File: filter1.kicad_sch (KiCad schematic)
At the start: 10 parts

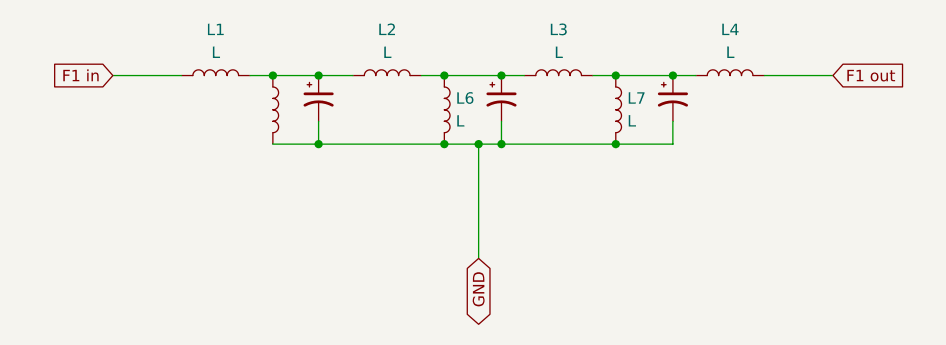
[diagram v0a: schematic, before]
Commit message: v0.2 passes ERC & DRC except for no solder mask between pads on SOT89
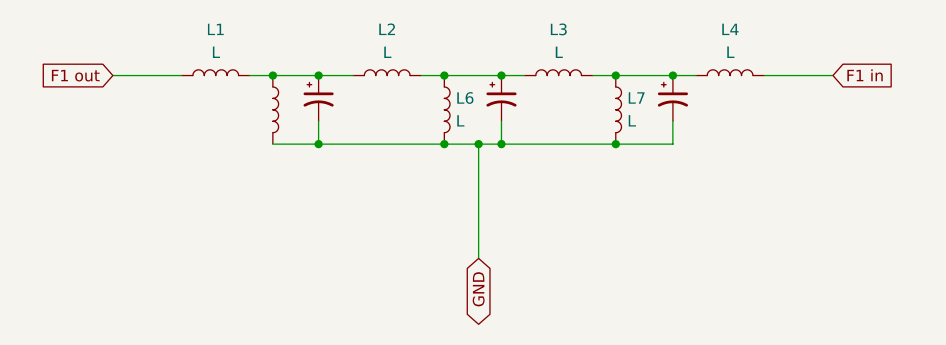
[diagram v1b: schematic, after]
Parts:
- C1, C2, C3: footprint (none) -> Capacitor_SMD:C_1210_3225Metric
- L1, L2, L3, L4, L5, L6, L7: footprint (none) -> Inductor_SMD:L_1210_3225Metric
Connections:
- net F1 in: now also L4.2; no longer L1.1
- net F1 out: now also L1.1; no longer L4.2
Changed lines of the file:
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@@
     )
   )
-  (global_label "F1 in" (shape input) (at 106.68 72.39 180) (fields_autoplaced)
+  (global_label "F1 out" (shape input) (at 106.68 72.39 180) (fields_autoplaced)
     (effects (font (size 1.27 1.27)) (justify right))
-    (property "Intersheetrefs" "${INTERSHEET_REFS}" (at 99.4089 72.39 0)
+    (property "Intersheetrefs" "${INTERSHEET_REFS}" (at 98.139 72.39 0)
       (effects (font (size 1.27 1.27)) (justify right) hide)
     )
   )
-  (global_label "F1 out" (shape input) (at 186.69 72.39 0) (fields_autoplaced)
+  (global_label "F1 in" (shape input) (at 186.69 72.39 0) (fields_autoplaced)
     (effects (font (size 1.27 1.27)) (justify left))
-    (property "Intersheetrefs" "${INTERSHEET_REFS}" (at 195.231 72.39 0)
+    (property "Intersheetrefs" "${INTERSHEET_REFS}" (at 193.9611 72.39 0)
       (effects (font (size 1.27 1.27)) (justify left) hide)
     )
@@
       (effects (font (size 1.27 1.27)))
     )
-    (property "Footprint" "" (at 137.16 72.39 0)
+    (property "Footprint" "Inductor_SMD:L_1210_3225Metric" (at 137.16 72.39 0)
       (effects (font (size 1.27 1.27)) hide)
     )
@@
       (effects (font (size 1.27 1.27)))
     )
-    (property "Footprint" "" (at 175.26 72.39 0)
+    (property "Footprint" "Inductor_SMD:L_1210_3225Metric" (at 175.26 72.39 0)
       (effects (font (size 1.27 1.27)) hide)
     )
@@
       (effects (font (size 1.27 1.27)))
     )
-    (property "Footprint" "" (at 156.21 72.39 0)
+    (property "Footprint" "Inductor_SMD:L_1210_3225Metric" (at 156.21 72.39 0)
       (effects (font (size 1.27 1.27)) hide)
     )
@@
       (effects (font (size 1.27 1.27)) (justify left) hide)
     )
-    (property "Footprint" "" (at 129.54 74.93 0)
+    (property "Footprint" "Capacitor_SMD:C_1210_3225Metric" (at 129.54 74.93 0)
       (effects (font (size 1.27 1.27)) hide)
     )
@@
       (effects (font (size 1.27 1.27)) (justify left) hide)
     )
-    (property "Footprint" "" (at 149.86 74.93 0)
+    (property "Footprint" "Capacitor_SMD:C_1210_3225Metric" (at 149.86 74.93 0)
       (effects (font (size 1.27 1.27)) hide)
     )
@@
       (effects (font (size 1.27 1.27)) (justify left))
     )
-    (property "Footprint" "" (at 143.51 76.2 0)
+    (property "Footprint" "Inductor_SMD:L_1210_3225Metric" (at 143.51 76.2 0)
       (effects (font (size 1.27 1.27)) hide)
     )
@@
       (effects (font (size 1.27 1.27)) (justify left) hide)
     )
-    (property "Footprint" "" (at 124.46 76.2 0)
+    (property "Footprint" "Inductor_SMD:L_1210_3225Metric" (at 124.46 76.2 0)
       (effects (font (size 1.27 1.27)) hide)
     )
@@
       (effects (font (size 1.27 1.27)) (justify left))
     )
-    (property "Footprint" "" (at 162.56 76.2 0)
+    (property "Footprint" "Inductor_SMD:L_1210_3225Metric" (at 162.56 76.2 0)
       (effects (font (size 1.27 1.27)) hide)
     )
@@
       (effects (font (size 1.27 1.27)) (justify left) hide)
     )
-    (property "Footprint" "" (at 168.91 74.93 0)
+    (property "Footprint" "Capacitor_SMD:C_1210_3225Metric" (at 168.91 74.93 0)
       (effects (font (size 1.27 1.27)) hide)
     )
@@
       (effects (font (size 1.27 1.27)))
     )
-    (property "Footprint" "" (at 118.11 72.39 0)
-      (effects (font (size 1.27 1.27)) hide)
-    )
+    (property "Footprint" "Inductor_SMD:L_1210_3225Metric" (at 118.11 72.39 0)
+      (effects (font (size 1.27 1.27)) hide)
+    )

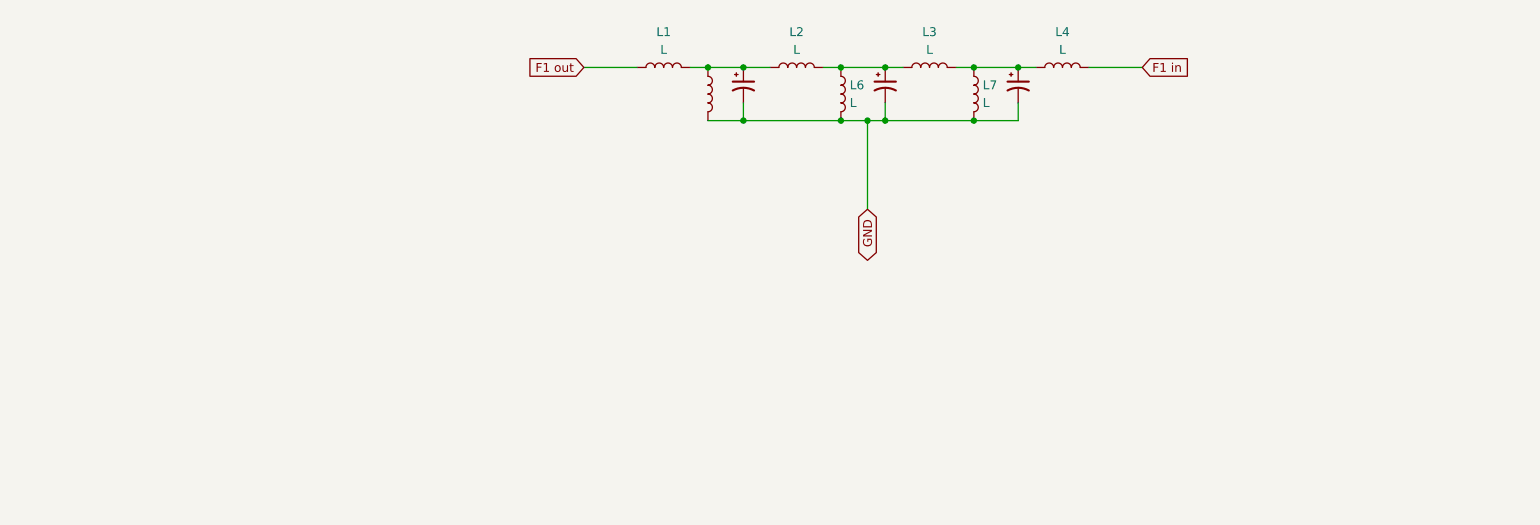
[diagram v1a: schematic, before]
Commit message: v0.3 added all four filters.  ERC pass, DRC struggling.  Need a ground plane
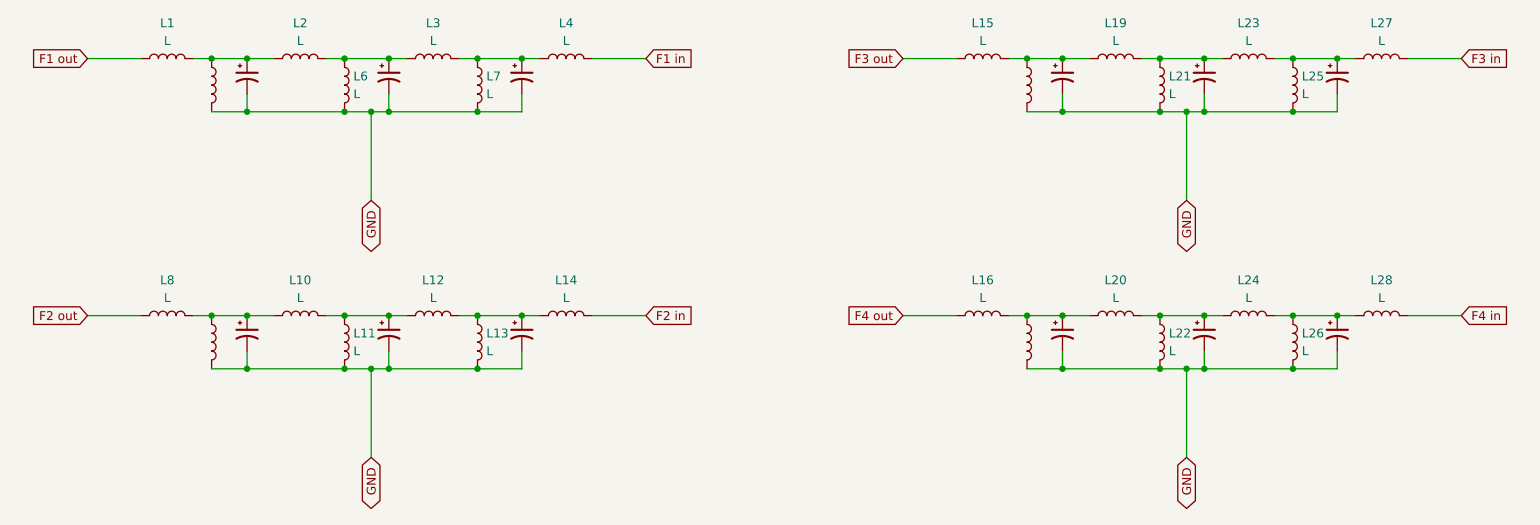
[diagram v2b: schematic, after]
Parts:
- added C10, C11, C12, C4, C5, C6, C7, C8, C9: C_Polarized_Small_US, Capacitor_SMD:C_1210_3225Metric, symbol Device:C_Polarized_Small_US
- added L10, L11, L12, L13, L14, L15, L16, L17, L18, L19, L20, L21, L22, L23, L24, L25, L26, L27, L28, L8, L9: L, Inductor_SMD:L_1210_3225Metric, symbol Device:L
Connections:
- net GND: now also C10.2, C11.2, C12.2, C4.2, C5.2, C6.2, C7.2, C8.2, C9.2, L11.2, L13.2, L17.2, L18.2, L21.2, L22.2, L25.2, L26.2, L9.2
- new net: C4.1, L10.1, L8.2, L9.1
- new net: C8.1, L16.2, L18.1, L20.1
- new net: C9.1, L19.2, L21.1, L23.1
- new net: C11.1, L23.2, L25.1, L27.1
- new net: C12.1, L24.2, L26.1, L28.1
- new net: C10.1, L20.2, L22.1, L24.1
- new net: C5.1, L10.2, L11.1, L12.1
- new net: C6.1, L12.2, L13.1, L14.1
- new net: C7.1, L15.2, L17.1, L19.1
- new net F2 in: L14.2
- new net F2 out: L8.1
- new net F3 in: L27.2
- new net F3 out: L15.1
- new net F4 in: L28.2
- new net F4 out: L16.1
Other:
- moved on the sheet: L1, L2, L3, L4, L6, L7

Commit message: v0.4 ERC/DRC pass; added missing caps; mounting holes; moved SMA & headers out and re-spaced filter chains
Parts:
- C1, C10, C11, C12, C2, C3, C4, C5, C6, C7, C8, C9: value C_Polarized_Small_US -> (none)
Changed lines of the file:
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@@
     (title "switched bandpass filter")
     (date "2023-07-22")
-    (rev "v0.3")
+    (rev "v0.4")
     (comment 1 "Copyright © 2023 WA7GIL")
   )
@@
       (effects (font (size 1.27 1.27)) (justify left) hide)
     )
-    (property "Value" "C_Polarized_Small_US" (at 177.8 111.3282 0)
+    (property "Value" " " (at 177.8 111.3282 0)
       (effects (font (size 1.27 1.27)) (justify left) hide)
     )
@@
       (effects (font (size 1.27 1.27)) (justify left) hide)
     )
-    (property "Value" "C_Polarized_Small_US" (at 198.12 74.4982 0)
+    (property "Value" " " (at 198.12 74.4982 0)
       (effects (font (size 1.27 1.27)) (justify left) hide)
     )
@@
       (effects (font (size 1.27 1.27)) (justify left) hide)
     )
-    (property "Value" "C_Polarized_Small_US" (at 217.17 111.3282 0)
+    (property "Value" " " (at 217.17 111.3282 0)
       (effects (font (size 1.27 1.27)) (justify left) hide)
     )
@@
       (effects (font (size 1.27 1.27)) (justify left) hide)
     )
-    (property "Value" "C_Polarized_Small_US" (at 100.33 111.3282 0)
+    (property "Value" " " (at 100.33 111.3282 0)
       (effects (font (size 1.27 1.27)) (justify left) hide)
     )
@@
       (effects (font (size 1.27 1.27)) (justify left) hide)
     )
-    (property "Value" "C_Polarized_Small_US" (at 217.17 74.4982 0)
+    (property "Value" " " (at 217.17 74.4982 0)
       (effects (font (size 1.27 1.27)) (justify left) hide)
     )
@@
       (effects (font (size 1.27 1.27)) (justify left) hide)
     )
-    (property "Value" "C_Polarized_Small_US" (at 60.96 74.4982 0)
+    (property "Value" " " (at 60.96 74.4982 0)
       (effects (font (size 1.27 1.27)) (justify left) hide)
     )
@@
       (effects (font (size 1.27 1.27)) (justify left) hide)
     )
-    (property "Value" "C_Polarized_Small_US" (at 81.28 74.4982 0)
+    (property "Value" " " (at 81.28 74.4982 0)
       (effects (font (size 1.27 1.27)) (justify left) hide)
     )
@@
       (effects (font (size 1.27 1.27)) (justify left) hide)
     )
-    (property "Value" "C_Polarized_Small_US" (at 81.28 111.3282 0)
+    (property "Value" " " (at 81.28 111.3282 0)
       (effects (font (size 1.27 1.27)) (justify left) hide)
     )
@@
       (effects (font (size 1.27 1.27)) (justify left) hide)
     )
-    (property "Value" "C_Polarized_Small_US" (at 100.33 74.4982 0)
+    (property "Value" " " (at 100.33 74.4982 0)
       (effects (font (size 1.27 1.27)) (justify left) hide)
     )
@@
       (effects (font (size 1.27 1.27)) (justify left) hide)
     )
-    (property "Value" "C_Polarized_Small_US" (at 60.96 111.3282 0)
+    (property "Value" " " (at 60.96 111.3282 0)
       (effects (font (size 1.27 1.27)) (justify left) hide)
     )
@@
       (effects (font (size 1.27 1.27)) (justify left) hide)
     )
-    (property "Value" "C_Polarized_Small_US" (at 177.8 74.4982 0)
+    (property "Value" " " (at 177.8 74.4982 0)
       (effects (font (size 1.27 1.27)) (justify left) hide)
     )
@@
       (effects (font (size 1.27 1.27)) (justify left) hide)
     )
-    (property "Value" "C_Polarized_Small_US" (at 198.12 111.3282 0)
-      (effects (font (size 1.27 1.27)) (justify left) hide)
-    )
+    (property "Value" " " (at 198.12 111.3282 0)
+      (effects (font (size 1.27 1.27)) (justify left) hide)
+    )
